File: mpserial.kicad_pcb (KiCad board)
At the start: 2 copper layers, 21 x 14 mm, 12 parts, among them J1 USB_A, Q1 Q_Photo_NPN, U1 FT230XS

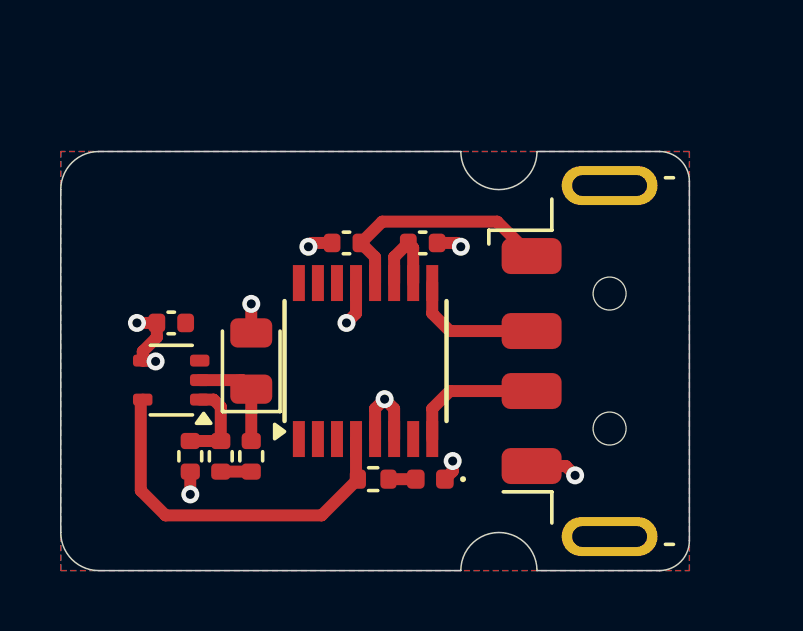
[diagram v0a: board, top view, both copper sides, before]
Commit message: corrected opamp footprint and symbol names, changed USB-A connector to throughhole for cheaper assembly
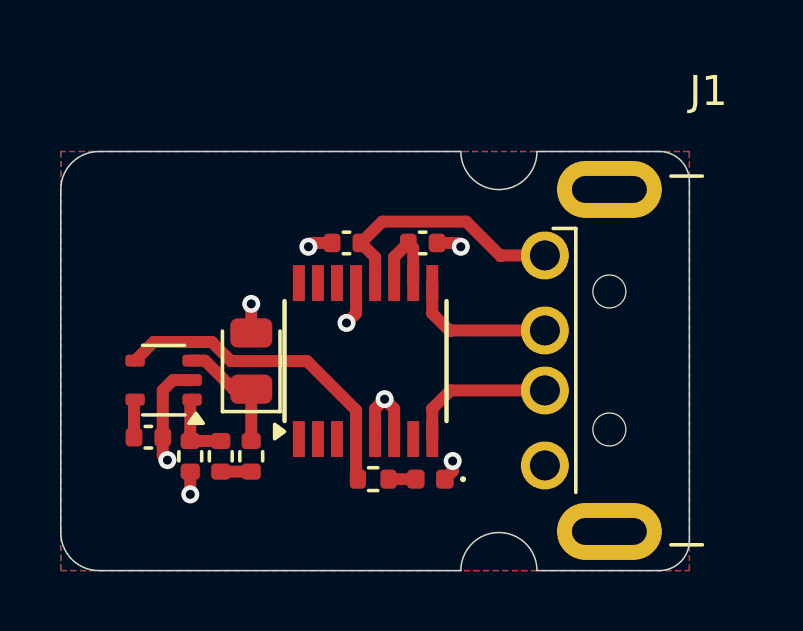
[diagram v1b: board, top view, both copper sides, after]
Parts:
- D1: value LED -> BLUE_LED
- J1: footprint Connector_USB:USB_A_Molex_48037-2200_Horizontal -> My Footprints:CONN_USB_A_MALE_HORIZONTAL_TH
- Q1: value Q_Photo_NPN -> RPM-075PT
- U2: value ~ -> LMV321
- moved J1 8.38 mm to (156.7, 88.9)
- moved C1 3.89 mm to (141.4, 91.4), turned to 0 degrees
- moved U2 0.25 mm to (141.9, 89.5)
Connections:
- U2 pad 2: Net-(Q1-C) -> GND
- U2 pad 3: +3V3 -> Net-(Q1-C)
- U2 pad 4: GND -> Net-(U1-RXD)
- U2 pad 5: Net-(U1-RXD) -> +3V3
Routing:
- net Net-(U1-RXD): track 12.5 -> 10.9 mm
- net +3V3: track 3.95 -> 5.22 mm
- net GND: track 12.6 -> 12.0 mm, vias 10 -> 8
- net Net-(U2-+): track 2.96 -> 2.42 mm
- net Net-(Q1-C): track 3.57 -> 4.09 mm
